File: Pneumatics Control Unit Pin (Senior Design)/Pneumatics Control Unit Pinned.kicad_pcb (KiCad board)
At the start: 4 copper layers, 123.4 x 83.7 mm, 100 parts, among them J1 RX_PORT, J10 Encoder, J11 Conn_01x02_Male, J12 Conn_01x02_Male, J13 Conn_01x02_Male, J14 Conn_01x02_Male, J15 Conn_01x02_Male, J16 Conn_01x02_Male, J17 Conn_01x02_Male, J18 Conn_01x02_Male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

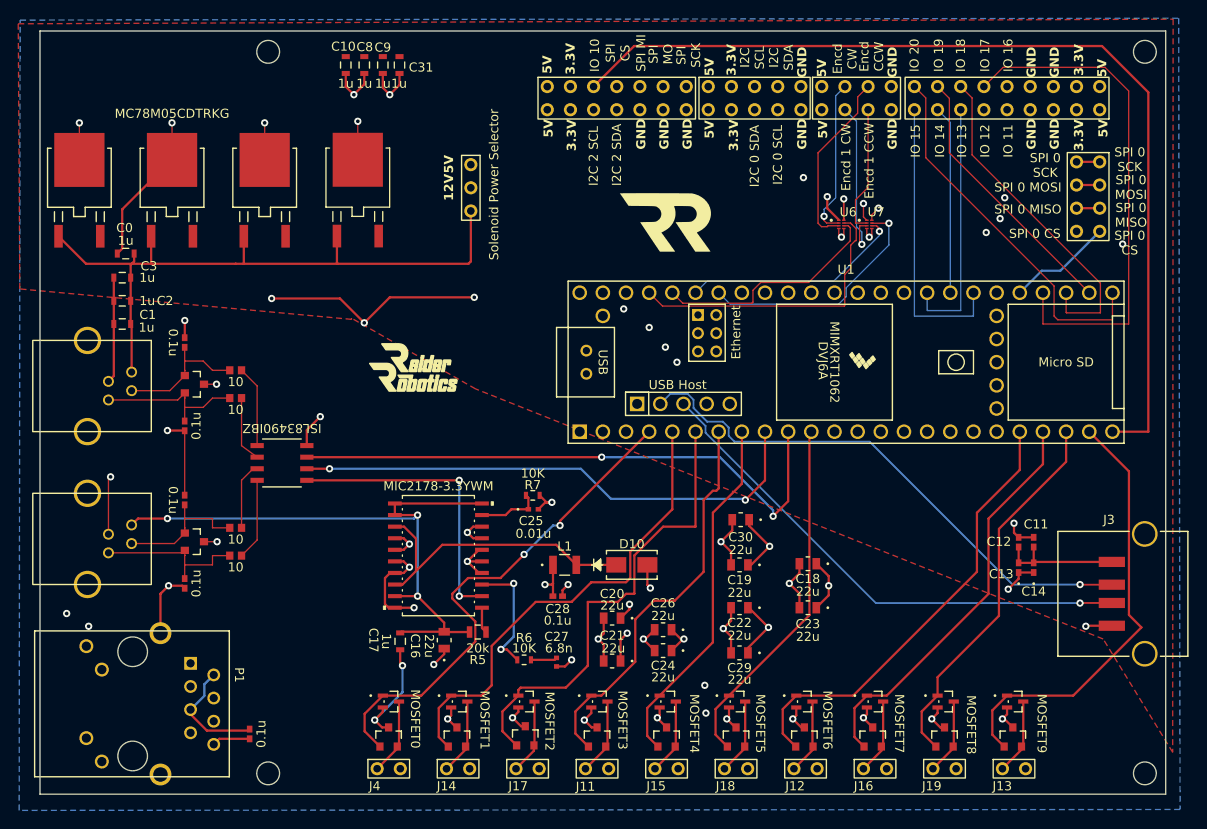
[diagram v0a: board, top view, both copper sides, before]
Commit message: Fixing the decoupling capacitor placement
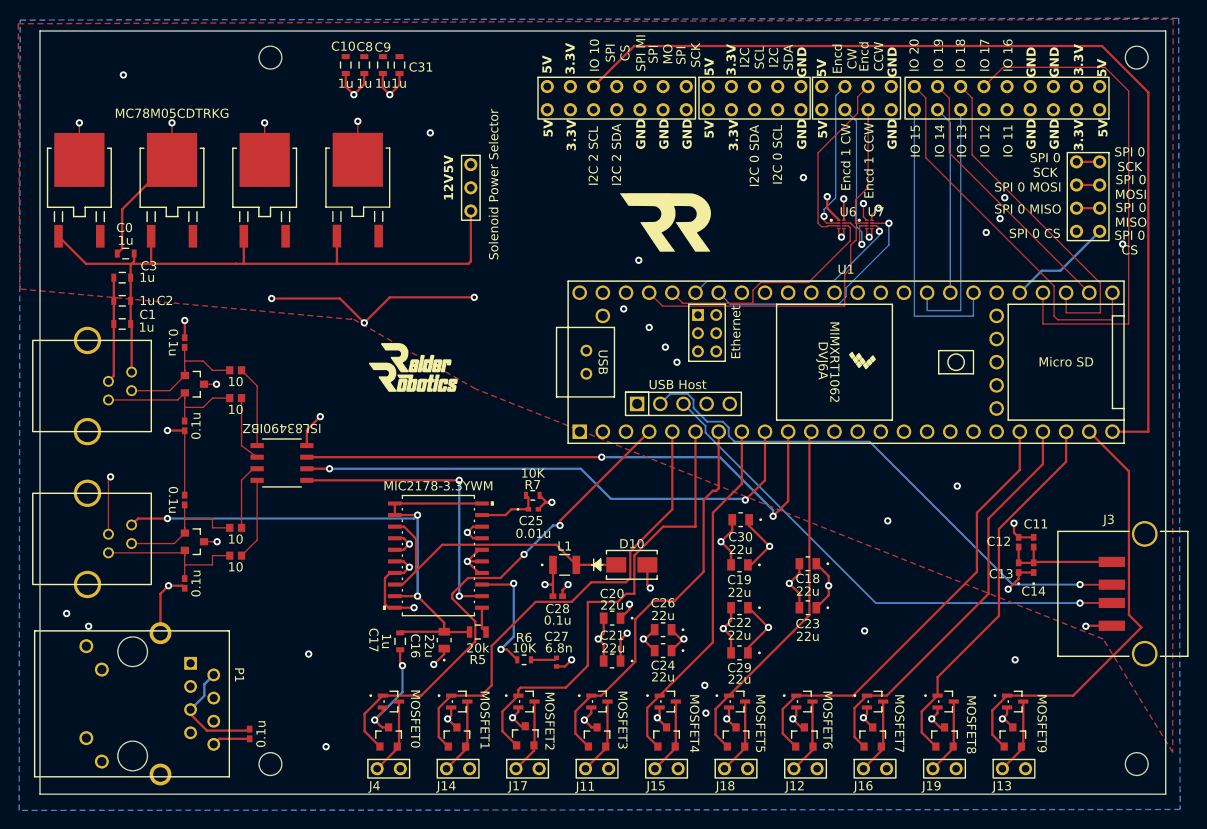
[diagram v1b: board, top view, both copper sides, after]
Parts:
- moved H1 1.35 mm to (149.2, 96.5)
- moved H4 1.27 mm to (54.0, 19.7)
- moved H2 1.20 mm to (54.6, 96.5)
- moved H3 1.09 mm to (149.2, 19.1)
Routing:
- net GND: vias 56 -> 65
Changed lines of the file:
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@@
   )
   (footprint "MountingHole:MountingHole_2.5mm" (layer "F.Cu")
-    (at 150.114 97.536)
+    (at 149.225 96.52)
     (descr "Mounting Hole 2.5mm, no annular")
     (tags "mounting hole 2.5mm no annular")
@@
     (fp_circle (center 0 0) (end 2.75 0)
       (stroke (width 0.05) (type solid)) (fill none) (layer "F.CrtYd"))
-    (pad "" np_thru_hole circle (at 0 0) (size 2.5 2.5) (drill 2.5) (layers *.Cu *.Mask))
+    (pad "" np_thru_hole circle (at 0 0) (size 2.5 2.5) (drill 2.5) (layers F&B.Cu *.Mask))
   )
   (footprint "Dual Diode:PESD1FLEX215" (layer "F.Cu")
@@
   )
   (footprint "MountingHole:MountingHole_2.5mm" (layer "F.Cu")
-    (at 53.975 97.536)
+    (at 54.61 96.52)
     (descr "Mounting Hole 2.5mm, no annular")
     (tags "mounting hole 2.5mm no annular")
@@
     (fp_circle (center 0 0) (end 2.75 0)
       (stroke (width 0.05) (type solid)) (fill none) (layer "F.CrtYd"))
-    (pad "" np_thru_hole circle (at 0 0) (size 2.5 2.5) (drill 2.5) (layers *.Cu *.Mask))
+    (pad "" np_thru_hole circle (at -0.385 0) (size 2.5 2.5) (drill 2.5) (layers F&B.Cu *.Mask))
   )
   (footprint "20K Res:SR1-0805-320" (layer "F.Cu")
@@
   )
   (footprint "MountingHole:MountingHole_2.5mm" (layer "F.Cu")
-    (at 150.114 18.415)
+    (at 149.225 19.05)
     (descr "Mounting Hole 2.5mm, no annular")
     (tags "mounting hole 2.5mm no annular")
@@
   )
   (footprint "MountingHole:MountingHole_2.5mm" (layer "F.Cu")
-    (at 53.975 18.415)
+    (at 53.975 19.685)
     (descr "Mounting Hole 2.5mm, no annular")
     (tags "mounting hole 2.5mm no annular")
@@
     (fp_circle (center 0 0) (end 2.75 0)
       (stroke (width 0.05) (type solid)) (fill none) (layer "F.CrtYd"))
-    (pad "" np_thru_hole circle (at 0 0) (size 2.5 2.5) (drill 2.5) (layers *.Cu *.Mask))
+    (pad "" np_thru_hole circle (at 0.25 -0.635) (size 2.5 2.5) (drill 2.5) (layers F&B.Cu *.Mask))
   )
   (footprint "0.1 uF Cap:0402YC104KAT2A" (layer "F.Cu")
@@
   (segment (start 77.089 73.025) (end 75.819 74.295) (width 0.25) (layer "F.Cu") (net 1))
   (via (at 31.877 80.01) (size 0.8) (drill 0.4) (layers "F.Cu" "B.Cu") (free) (net 1))
+  (via (at 94.615 41.275) (size 0.8) (drill 0.4) (layers "F.Cu" "B.Cu") (net 1))
   (via (at 86.868 76.835) (size 0.8) (drill 0.4) (layers "F.Cu" "B.Cu") (net 1))
   (via (at 96.647 91.44) (size 0.8) (drill 0.4) (layers "F.Cu" "B.Cu") (net 1))
@@
   (via (at 69.977 79.375) (size 0.8) (drill 0.4) (layers "F.Cu" "B.Cu") (net 1))
   (via (at 92.964 46.609) (size 0.8) (drill 0.4) (layers "F.Cu" "B.Cu") (free) (net 1))
+  (via (at 60.325 94.615) (size 0.8) (drill 0.4) (layers "F.Cu" "B.Cu") (net 1))
   (via (at 108.966 72.644) (size 0.8) (drill 0.4) (layers "F.Cu" "B.Cu") (net 1))
   (via (at 72.136 85.598) (size 0.8) (drill 0.4) (layers "F.Cu" "B.Cu") (net 1))
@@
   (via (at 43.428283 26.201433) (size 0.8) (drill 0.4) (layers "F.Cu" "B.Cu") (net 1))
   (via (at 69.469 72.39) (size 0.8) (drill 0.4) (layers "F.Cu" "B.Cu") (net 1))
+  (via (at 135.89 85.09) (size 0.8) (drill 0.4) (layers "F.Cu" "B.Cu") (net 1))
   (via (at 48.313913 54.864) (size 0.8) (drill 0.4) (layers "F.Cu" "B.Cu") (net 1))
   (via (at 43.053 76.962) (size 0.8) (drill 0.4) (layers "F.Cu" "B.Cu") (net 1))
@@
   (via (at 108.839 81.534) (size 0.8) (drill 0.4) (layers "F.Cu" "B.Cu") (net 1))
   (via (at 75.819 71.12) (size 0.8) (drill 0.4) (layers "F.Cu" "B.Cu") (net 1))
+  (via (at 129.54 66.04) (size 0.8) (drill 0.4) (layers "F.Cu" "B.Cu") (net 1))
+  (via (at 38.1 20.955) (size 0.8) (drill 0.4) (layers "F.Cu" "B.Cu") (net 1))
   (via (at 59.69 58.42) (size 0.8) (drill 0.4) (layers "F.Cu" "B.Cu") (net 1))
+  (via (at 58.42 84.455) (size 0.8) (drill 0.4) (layers "F.Cu" "B.Cu") (net 1))
   (via (at 42.926 59.944) (size 0.8) (drill 0.4) (layers "F.Cu" "B.Cu") (net 1))
   (via (at 88.646 91.694) (size 0.8) (drill 0.4) (layers "F.Cu" "B.Cu") (net 1))
@@
   (via (at 33.273896 26.205853) (size 0.8) (drill 0.4) (layers "F.Cu" "B.Cu") (net 1))
   (via (at 85.09 67.818) (size 0.8) (drill 0.4) (layers "F.Cu" "B.Cu") (net 1))
+  (via (at 121.92 69.85) (size 0.8) (drill 0.4) (layers "F.Cu" "B.Cu") (net 1))
   (via (at 95.758 48.641) (size 0.8) (drill 0.4) (layers "F.Cu" "B.Cu") (free) (net 1))
   (via (at 98.806 52.451) (size 0.8) (drill 0.4) (layers "F.Cu" "B.Cu") (free) (net 1))
@@
   (via (at 126.746 91.567) (size 0.8) (drill 0.4) (layers "F.Cu" "B.Cu") (net 1))
   (via (at 99.568 82.804) (size 0.8) (drill 0.4) (layers "F.Cu" "B.Cu") (net 1))
+  (via (at 71.755 27.305) (size 0.8) (drill 0.4) (layers "F.Cu" "B.Cu") (net 1))
   (via (at 104.267 91.567) (size 0.8) (drill 0.4) (layers "F.Cu" "B.Cu") (net 1))
+  (via (at 119.38 81.915) (size 0.8) (drill 0.4) (layers "F.Cu" "B.Cu") (net 1))
   (via (at 134.493 91.567) (size 0.8) (drill 0.4) (layers "F.Cu" "B.Cu") (net 1))
   (via (at 95.885 77.216) (size 0.8) (drill 0.4) (layers "F.Cu" "B.Cu") (net 1))

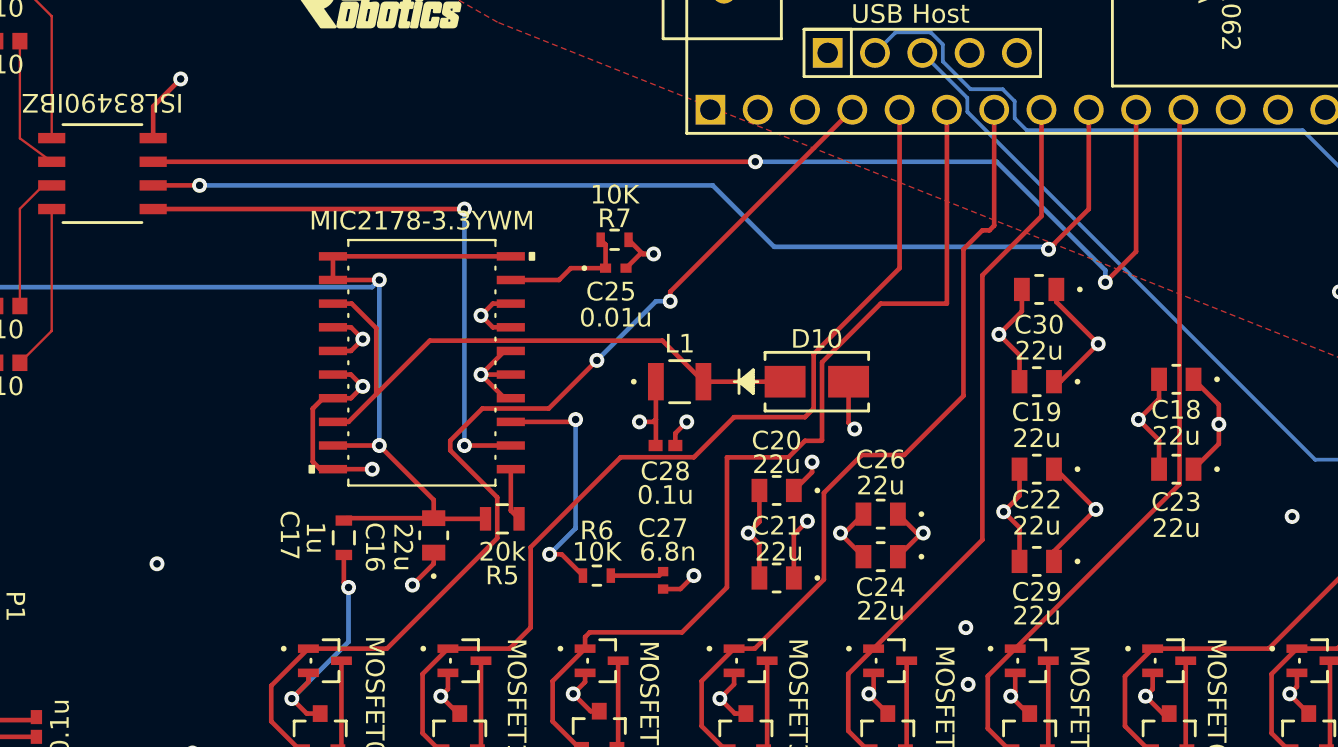
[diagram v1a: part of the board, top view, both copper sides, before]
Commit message: Moving the caps, so they decouple
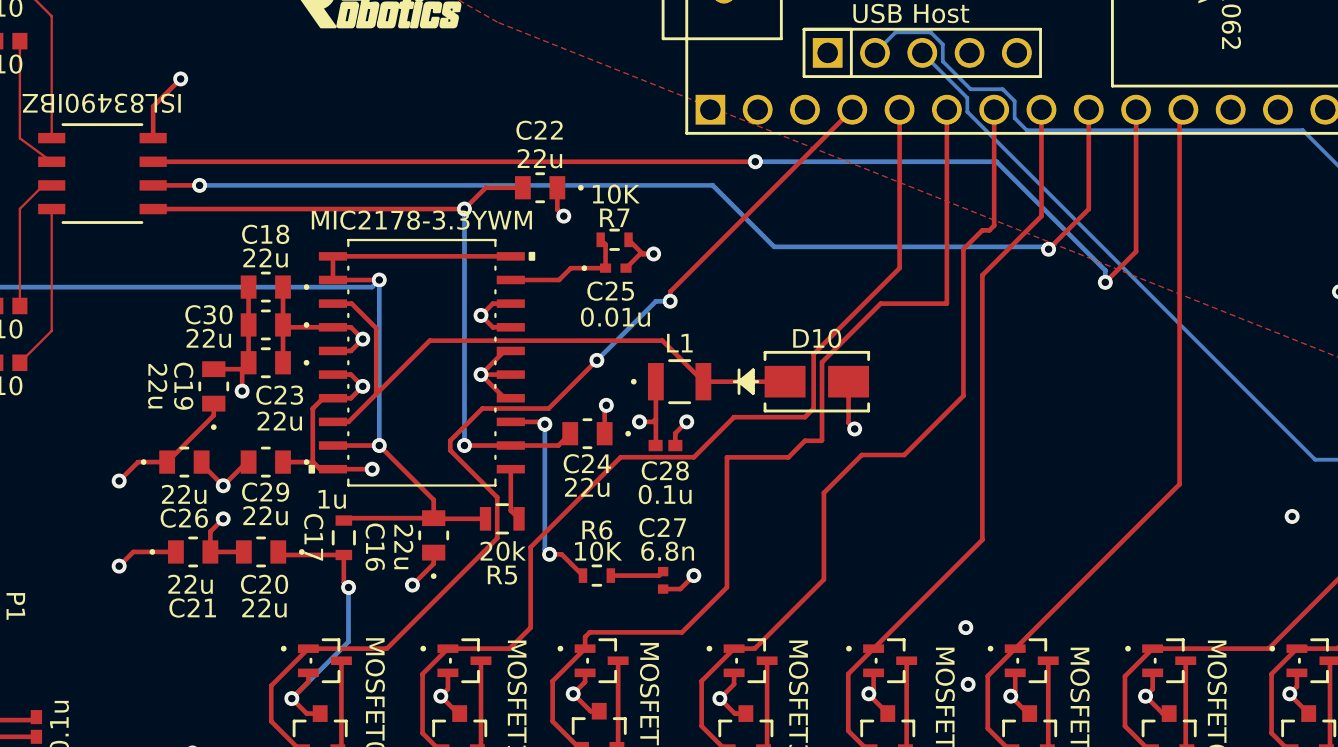
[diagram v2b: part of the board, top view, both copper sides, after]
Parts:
- moved C23 49.2 mm to (64.3, 73.7)
- moved C18 49.1 mm to (64.3, 69.6)
- moved C19 44.2 mm to (61.5, 74.9), turned to 90 degrees
- moved C29 41.7 mm to (64.3, 79.0)
- moved C30 41.6 mm to (64.3, 71.6)
- moved C26 37.5 mm to (59.9, 79.0), turned to 0 degrees
- moved C21 31.4 mm to (60.4, 83.8), turned to 0 degrees
- moved C22 30.7 mm to (79.0, 64.3)
- moved C20 27.9 mm to (64.0, 83.8)
- moved C24 17.1 mm to (81.5, 77.5)
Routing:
- net +3V3: track 67.3 -> 63.1 mm, vias 10 -> 8
- net GND: track 245.7 -> 242.7 mm, vias 65 -> 62
- net Net-(U8-COMP): track 13.6 -> 11.2 mm
